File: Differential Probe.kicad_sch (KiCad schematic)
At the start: 54 parts, among them J1 Conn_Coaxial, J2 Conn_Coaxial, J3 Conn_Coaxial, U1 OPA810xD, U2 OPA810xD, U3 OPA810xD

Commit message: Next work push
added callculator for instrumental ampl
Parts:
- added C25: 10n, Capacitor_SMD:C_0603_1608Metric_Pad1.08x0.95mm_HandSolder, symbol Device:C
- added C26: 100n, Capacitor_SMD:C_0603_1608Metric_Pad1.08x0.95mm_HandSolder, symbol Device:C
- added C27: 4u7, Capacitor_SMD:C_0805_2012Metric_Pad1.18x1.45mm_HandSolder, symbol Device:C
- added D3: D_Dual_CommonAnode_AKK, Package_TO_SOT_SMD:TSOT-23, symbol Device:D_Dual_CommonAnode_AKK
- added F1: Fuse, Fuse:Fuse_1206_3216Metric_Pad1.42x1.75mm_HandSolder, symbol Device:Fuse
- added FB1: 600 OHM, Inductor_SMD:L_1206_3216Metric_Pad1.22x1.90mm_HandSolder, symbol Device:FerriteBead
- added J4: USB_C_Receptacle_PowerOnly_6P, Connector_USB:USB_C_Receptacle_GCT_USB4125-xx-x-0190_6P_TopMnt_Horizontal, symbol Connector:USB_C_Receptacle_PowerOnly_6P
- added R23: 2, Resistor_SMD:R_0603_1608Metric_Pad0.98x0.95mm_HandSolder, symbol Device:R
- added R24: 22, Resistor_SMD:R_0603_1608Metric_Pad0.98x0.95mm_HandSolder, symbol Device:R
- added R25, R26: 5k1, Resistor_SMD:R_0603_1608Metric_Pad0.98x0.95mm_HandSolder, symbol Device:R
- added SW1: SW_SP3T_NINGI, Library:SR17A1320F39N, symbol New_Library:SW_SP3T_NINGI
- R15, R16, R17, R18, R20, R21: value 1k -> 100
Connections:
- net at C17.2, R21.1, U1.2 (-): now also SW1.1 (Common), SW1.10 (Common)
- net at C18.1, R20.2, U2.2 (-): now also R23.1, R24.1
- new net: C26.1, C27.1, FB1.2
- new net: C25.1, D3.3 (K), F1.2, FB1.1
- new net: R24.2, SW1.3
- new net: R23.2, SW1.4
- new net: J4.A5 (CC1), R26.1
- new net: F1.1, J4.A9 (VBUS), J4.B9 (VBUS)
- new net: J4.B5 (CC2), R25.1
- new net GND: C25.2, C26.2, C27.2, D3.2 (K), J4.A12 (GND), J4.B12 (GND), J4.S1 (SHIELD), R25.2, R26.2
- no-connect marks 0 -> 2
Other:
- moved on the sheet: J1, R15, R16, R17, R18, R19, R22, U3

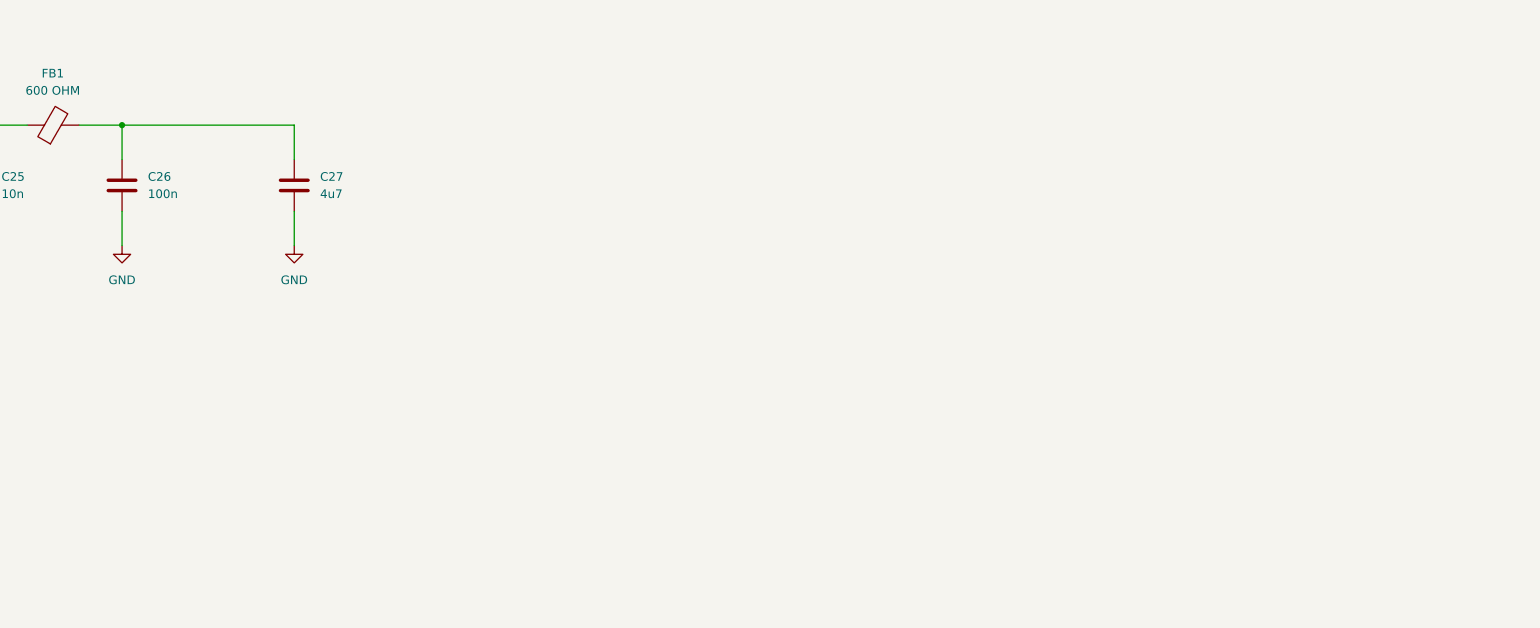
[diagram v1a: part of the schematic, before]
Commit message: battery circuit added
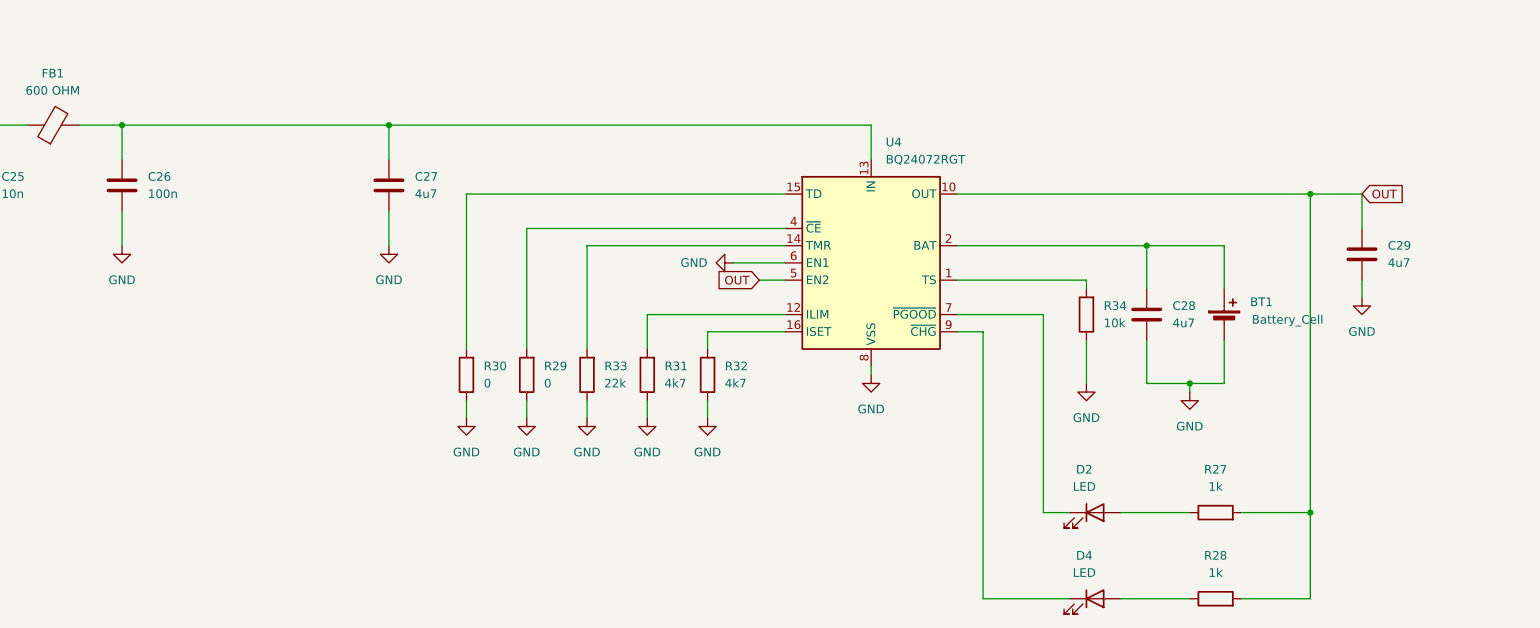
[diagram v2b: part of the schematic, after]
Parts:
- added BT1: Battery_Cell, symbol Device:Battery_Cell
- added C28, C29: 4u7, Capacitor_SMD:C_0805_2012Metric_Pad1.18x1.45mm_HandSolder, symbol Device:C
- added D2, D4: LED, Diode_SMD:D_0603_1608Metric_Pad1.05x0.95mm_HandSolder, symbol Device:LED
- added R27, R28: 1k, Resistor_SMD:R_0603_1608Metric_Pad0.98x0.95mm_HandSolder, symbol Device:R
- added R29, R30: 0, Resistor_SMD:R_0603_1608Metric_Pad0.98x0.95mm_HandSolder, symbol Device:R
- added R31, R32: 4k7, Resistor_SMD:R_0603_1608Metric_Pad0.98x0.95mm_HandSolder, symbol Device:R
- added R33: 22k, Resistor_SMD:R_0603_1608Metric_Pad0.98x0.95mm_HandSolder, symbol Device:R
- added R34: 10k, Resistor_SMD:R_0603_1608Metric_Pad0.98x0.95mm_HandSolder, symbol Device:R
- added U4: BQ24072RGT, Package_DFN_QFN:VQFN-16-1EP_3x3mm_P0.5mm_EP1.6x1.6mm, symbol Battery_Management:BQ24072RGT
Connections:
- net GND: now also BT1.2 (-), C28.2, C29.2, R29.1, R30.1, R31.1, R32.1, R33.1, R34.1, U4.17 (VSS), U4.6 (EN1), U4.8 (VSS)
- net at C26.1, C27.1, FB1.2: now also U4.13 (IN)
- new net: R29.2, U4.4 (~{CE})
- new net: R34.2, U4.1 (TS)
- new net: BT1.1 (+), C28.1, U4.2 (BAT), U4.3 (BAT)
- new net: R31.2, U4.12 (ILIM)
- new net: R33.2, U4.14 (TMR)
- new net: R30.2, U4.15 (TD)
- new net: R32.2, U4.16 (ISET)
- new net: D2.1 (K), U4.7 (~{PGOOD})
- new net: D4.1 (K), U4.9 (~{CHG})
- new net: D4.2 (A), R28.1
- new net: D2.2 (A), R27.1
- new net OUT: C29.1, R27.2, R28.2, U4.10 (OUT), U4.11 (OUT), U4.5 (EN2)
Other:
- moved on the sheet: C27

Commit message: Layout started
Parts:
- added C17: 100u, Capacitor_Tantalum_SMD:CP_EIA-6032-28_Kemet-C_Pad2.25x2.35mm_HandSolder, symbol Device:C_Polarized
- added C31, C38, C39, C44, C45: 22u, Capacitor_SMD:C_1210_3225Metric, symbol Device:C
- added C32, C33, C36, C37, C40, C41, C42, C43: 100n, Capacitor_SMD:C_1206_3216Metric_Pad1.33x1.80mm_HandSolder, symbol Device:C
- added C34, C35: 10p, Capacitor_SMD:C_1206_3216Metric_Pad1.33x1.80mm_HandSolder, symbol Device:C
- added L1: 4u7, Inductor_SMD:L_1008_2520Metric_Pad1.43x2.20mm_HandSolder, symbol Device:L_Ferrite
- added R35: 464k, Resistor_SMD:R_0603_1608Metric_Pad0.98x0.95mm_HandSolder, symbol Device:R
- added R36: 121k, Resistor_SMD:R_0603_1608Metric_Pad0.98x0.95mm_HandSolder, symbol Device:R
- added R37: 590k, Resistor_SMD:R_0603_1608Metric_Pad0.98x0.95mm_HandSolder, symbol Device:R
- added R38, R39, R40, R41: 0, Resistor_SMD:R_0603_1608Metric_Pad0.98x0.95mm_HandSolder, symbol Device:R
- added U5: TPS65135RTER, Library:QFN50P300X300X80-17N, symbol TPS65135RTER:TPS65135RTER
- BT1: value Battery_Cell -> 18650; footprint (none) -> Battery:BatteryHolder_MPD_BH-18650-PC2
- C27: renamed from C17; footprint Capacitor_SMD:C_1206_3216Metric_Pad1.33x1.80mm_HandSolder -> Capacitor_SMD:C_0603_1608Metric_Pad1.08x0.95mm_HandSolder
- C28: renamed from C18; footprint Capacitor_SMD:C_1206_3216Metric_Pad1.33x1.80mm_HandSolder -> Capacitor_SMD:C_0603_1608Metric_Pad1.08x0.95mm_HandSolder
- renumbered C21 to C1, C8 to C10, C25 to C11, C7 to C12, C4 to C13, C6 to C14, C5 to C15, C26 to C16, C14 to C18, C13 to C19, C22 to C2, C27 to C20, C15 to C21, C11 to C22, C16 to C23, C12 to C24, C23 to C25, C24 to C26, C28 to C29, C20 to C3, C29 to C30, C19 to C4, C10 to C5, C1 to C6, C9 to C7, C2 to C8, C3 to C9, D3 to D1, D1 to D2, D2 to D3, J2 to J1, J3 to J2, J4 to J3, J1 to J4, R25 to R1, R9 to R10, R5 to R11, R10 to R12, R12 to R13, R11 to R14, R14 to R15, R13 to R16, R30 to R17, R29 to R18, R33 to R19, R26 to R2, R31 to R20, R32 to R21, R21 to R22, R20 to R23, R34 to R24, R27 to R25, R28 to R26, R23 to R27, R24 to R28, R15 to R29, R1 to R3, R17 to R30, R16 to R31, R18 to R32, R19 to R33, R22 to R34, R6 to R4, R2 to R5, R7 to R6, R3 to R7, R4 to R9, U4 to U1, U1 to U2, U2 to U3, U3 to U4
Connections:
- net +6V: now also C36.1, C40.1, C42.1, C44.1, R40.1
- net -6V: now also C37.2, C41.2, C43.2, C45.2, R41.1
- net GND: now also C17.2, C31.2, C32.2, C33.2, C38.2, C39.1, C44.2, C45.1, U5.11 (PGND), U5.12 (PGND), U5.17 (EXP), U5.5 (GND)
- net OUT: now also C31.1, C32.1, U5.1 (VIN), U5.8 (EN)
- net at C16.1, C20.1, FB1.2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: now also C17.1
- new net: C36.2, C37.1, C40.2, C41.1, C42.2, C43.1
- new net: C38.1, R38.1, R40.2
- new net: C34.1, R35.2, R38.2, U5.10 (OUTP), U5.9 (OUTP)
- new net: C33.1, U5.4 (VAUX)
- new net: C39.2, R39.1, R41.2
- new net: C35.1, R36.1, R37.2, U5.6 (FBG)
- new net: C35.2, R37.1, R39.2, U5.2 (OUTN), U5.3 (OUTN)
- new net: L1.2, U5.13 (L2), U5.14 (L2)
- new net: L1.1, U5.15 (L1), U5.16 (L1)
- new net: C34.2, R35.1, R36.2, U5.7 (FB)
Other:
- note added: "2x RC filter"
- note added: "Battery Managment"
- note added: "DC/DC"
- note added: "USB INPUT"
- moved on the sheet: BT1, C1, C10, C11, C12, C13, C14, C15, C16, C18, C19, C2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

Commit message: PCB layout 90%
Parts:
- removed C1, C2, C3, C4: 10p, Capacitor_SMD:C_1206_3216Metric_Pad1.33x1.80mm_HandSolder, symbol Device:C
- removed J1, J2: Conn_Coaxial, Connector_Coaxial:BNC_Amphenol_B6252HB-NPP3G-50_Horizontal, symbol Connector:Conn_Coaxial
- removed SW1: SW_SP3T_NINGI, Library:SR17A1320F39N, symbol New_Library:SW_SP3T_NINGI
- added C46, C47, C48, C49: 10p, Capacitor_SMD:C_1206_3216Metric_Pad1.33x1.80mm_HandSolder, symbol Device:C
- added C50, C51: 4u7, Capacitor_SMD:C_0603_1608Metric_Pad1.08x0.95mm_HandSolder, symbol Device:C
- added H1, H2, H3, H4, H5: MountingHole_Pad, MountingHole:MountingHole_3.2mm_M3_DIN965_Pad, symbol Mechanical:MountingHole_Pad
- added J1, J2: Conn_01x01_Pin, NetTie:NetTie-2_SMD_Pad2.0mm, symbol Connector:Conn_01x01_Pin
- added R42: 200, Resistor_SMD:R_0603_1608Metric_Pad0.98x0.95mm_HandSolder, symbol Device:R
- added SW2: SW_DIP_x03, Button_Switch_SMD:SW_DIP_SPSTx03_Slide_KingTek_DSHP03TS_W7.62mm_P1.27mm, symbol Switch:SW_DIP_x03
- C20, C29, C30: footprint Capacitor_SMD:C_0805_2012Metric_Pad1.18x1.45mm_HandSolder -> Capacitor_SMD:C_0603_1608Metric_Pad1.08x0.95mm_HandSolder
- C32, C33, C34, C35, C36, C37, C40, C41, C42, C43: footprint Capacitor_SMD:C_1206_3216Metric_Pad1.33x1.80mm_HandSolder -> Capacitor_SMD:C_0603_1608Metric_Pad1.08x0.95mm_HandSolder
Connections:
- net GNDA is gone; now on net GND: C18.2, C19.1, C21.2, C22.1, C23.2, C24.1, C25.2, C26.1, J4.2 (Ext), R31.2, RV1.2
- net GND: now also C36.2, C37.1, C40.2, C41.1, C42.2, C43.1, C47.2, C48.1, C50.2, C51.1, H1.1, H2.1, H3.1, H4.1, H5.1
- net at C27.2, R22.1, U2.2 (-): now also SW2.1, SW2.2, SW2.3
- net at C34.1, R35.2, R38.2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: now also C50.1
- net at C6.1, R4.1: now also C49.2, J2.1 (Pin_1)
- net at R28.2: now also SW2.5
- net at R27.2: now also SW2.4
- net at C28.1, R23.2, R27.1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: now also R42.1
- net at C35.2, R37.1, R39.2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: now also C51.2
- net at C5.2, R3.1: now also C46.1, J1.1 (Pin_1)
- new net: C46.2, C47.1
- new net: R42.2, SW2.6
- new net: C48.2, C49.1
- no-connect marks 2 -> 1
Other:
- note added: "300V"
- note removed: "150V"
- moved on the sheet: BT1, C10, C11, C16, C17, C20, C29, C30, C31, C32, C33, C34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

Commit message: Ready to check
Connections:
- net GND: no longer C47.2, C48.1, H1.1
- new net Earth: C47.2, C48.1, H1.1
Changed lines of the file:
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@@
 	(text "CM filter"
 		(exclude_from_sim no)
-		(at 110.49 119.888 0)
+		(at 104.394 116.586 0)
 		(effects
 			(font
@@
 	(wire
 		(pts
+			(xy 95.25 119.38) (xy 100.33 119.38)
+		)
+		(stroke
+			(width 0)
+			(type default)
+		)
+	)
+	(wire
+		(pts
 			(xy 509.27 106.68) (xy 509.27 107.95)
 		)
@@
 	)
 	(symbol
-		(lib_id "power:GNDA")
-		(at 95.25 119.38 90)
-		(unit 1)
-		(exclude_from_sim no)
-		(in_bom yes)
-		(on_board yes)
-		(dnp no)
-		(fields_autoplaced yes)
-		(property "Reference" "#PWR047"
-			(at 101.6 119.38 0)
-			(effects
-				(font
-					(size 1.27 1.27)
-				)
-				(hide yes)
-			)
-		)
-		(property "Value" "GNDA"
-			(at 99.06 119.3799 90)
-			(effects
-				(font
-					(size 1.27 1.27)
-				)
-				(justify right)
-			)
-		)
-		(property "Footprint" ""
-			(at 95.25 119.38 0)
-			(effects
-				(font
-					(size 1.27 1.27)
-				)
-				(hide yes)
-			)
-		)
-		(property "Datasheet" ""
-			(at 95.25 119.38 0)
-			(effects
-				(font
-					(size 1.27 1.27)
-				)
-				(hide yes)
-			)
-		)
-		(property "Description" "Power symbol creates a global label with name \"GNDA\" , analog ground"
-			(at 95.25 119.38 0)
-			(effects
-				(font
-					(size 1.27 1.27)
-				)
-				(hide yes)
-			)
-		)
-		(pin "1"
-		)
-		(instances
-			(project "Differential Probe"
-				(path "/cddaf0d8-edb3-4ae6-9925-48ad9a69f40b"
-					(reference "#PWR047")
-					(unit 1)
-				)
-			)
-		)
-	)
-	(symbol
 		(lib_id "Device:C")
 		(at 480.06 254 0)
@@
 					(unit 1)
 				)
+			)
+		)
+	)
+	(symbol
+		(lib_id "power:Earth")
+		(at 100.33 119.38 90)
+		(unit 1)
+		(exclude_from_sim no)
+		(in_bom yes)
+		(on_board yes)
+		(dnp no)
+		(fields_autoplaced yes)
+		(property "Reference" "#PWR03"
+			(at 106.68 119.38 0)
+			(effects
+				(font
+					(size 1.27 1.27)
+				)
+				(hide yes)
+			)
+		)
+		(property "Value" "Earth"
+			(at 104.14 119.3799 90)
+			(effects
+				(font
+					(size 1.27 1.27)
+				)
+				(justify right)
+			)
+		)
+		(property "Footprint" ""
+			(at 100.33 119.38 0)
+			(effects
+				(font
+					(size 1.27 1.27)
+				)
+				(hide yes)
+			)
+		)
+		(property "Datasheet" "~"
+			(at 100.33 119.38 0)
+			(effects
+				(font
+					(size 1.27 1.27)
+				)
+				(hide yes)
+			)
+		)
+		(property "Description" "Power symbol creates a global label with name \"Earth\""
+			(at 100.33 119.38 0)
+			(effects
+				(font
+					(size 1.27 1.27)
+				)
+				(hide yes)
+			)
+		)
+		(pin "1"
+		)
+		(instances
+			(project ""
+				(path "/cddaf0d8-edb3-4ae6-9925-48ad9a69f40b"
+					(reference "#PWR03")
+					(unit 1)
+				)

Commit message: Done
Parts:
- added C52: 100n, Capacitor_SMD:C_0603_1608Metric_Pad1.08x0.95mm_HandSolder, symbol Device:C
- added SW1: EG1218, Button_Switch_THT:SW_Slide-03_Wuerth-WS-SLTV_10x2.5x6.4_P2.54mm, symbol Switch:SW_Wuerth_450301014042
- BT1: value 18650 -> LiPo; footprint Battery:BatteryHolder_MPD_BH-18650-PC2 -> Connector_PinHeader_2.00mm:PinHeader_1x02_P2.00mm_Vertical
- J4: footprint Connector_Coaxial:BNC_Amphenol_B6252HB-NPP3G-50_Horizontal -> Library:BNC_Molex_73100-0154-50_Horizontal
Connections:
- net GND: now also C52.2
- net OUT: now also SW1.2 (C); no longer C31.1, C32.1, U5.1 (VIN), U5.8 (EN)
- new net: C31.1, C32.1, C52.1, SW1.1 (B), U5.1 (VIN), U5.8 (EN)
- no-connect marks 1 -> 2
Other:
- note added: "150V"
- note removed: "300V"
- company: Michal Karas -> Michal Karas&Aleksander Kaweczynski
- moved on the sheet: C31, C32
